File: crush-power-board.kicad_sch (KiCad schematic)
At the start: 17 parts, among them J1 Barrel_Jack, J2 1x2 Header, J3 Molex Micro Fit 3.0, J4 2157601008, J5 XT90PW-F

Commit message: Changed 5V regulator and 12V regulator to the SiC461. Both support 10A and 5V and 12V respectively
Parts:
- renumbered D3 to D1, D5 to D2, D4 to D3, D6 to D4, J5 to J1, J1 to J4, J4 to J5, R25 to R1, R28 to R2, R26 to R3, R27 to R4
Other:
- sheet 12V Regulator ports: added V_IN; removed 5V_IN, PGOOD_12V, VIN
- sheet 3.3V Regulator ports: added V_IN; removed Vin
- sheet 3.3V Regulator Thruster Side ports: added V_IN; removed Vin
- sheet 5V Regulator ports: added V_IN; removed PGOOD_5V, Vin

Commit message: Added more to the layout of the 12V regulator as well as changed some capacitor footprints
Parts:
- J2: footprint Connector_PinHeader_2.54mm:PinHeader_1x02_P2.54mm_Horizontal -> Connector_PinHeader_2.54mm:PinHeader_1x02_P2.54mm_Vertical
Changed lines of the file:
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@@
       (effects (font (size 1.27 1.27)))
     )
-    (property "Footprint" "Connector_PinHeader_2.54mm:PinHeader_1x02_P2.54mm_Horizontal" (at 73.66 129.54 0)
+    (property "Footprint" "Connector_PinHeader_2.54mm:PinHeader_1x02_P2.54mm_Vertical" (at 73.66 129.54 0)
       (effects (font (size 1.27 1.27)) hide)
     )

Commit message: fix batt_t planes
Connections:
- net +BATT: no longer J5.6
- net GND: no longer J5.8, R2.2
- new net +BATT_T: J5.6
- new net GND1: J5.8, R2.2
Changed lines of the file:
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@@
-    )
-  )
-  (symbol (lib_id "power:GND") (at 135.89 135.89 0) (unit 1)
-    (in_bom yes) (on_board yes) (dnp no) (fields_autoplaced)
-    (property "Reference" "#PWR018" (at 135.89 142.24 0)
-      (effects (font (size 1.27 1.27)) hide)
-    )
-    (property "Value" "GND_T" (at 135.89 140.97 0)
-      (effects (font (size 1.27 1.27)))
-    )
-    (property "Footprint" "" (at 135.89 135.89 0)
-      (effects (font (size 1.27 1.27)) hide)
-    )
-    (property "Datasheet" "" (at 135.89 135.89 0)
-      (effects (font (size 1.27 1.27)) hide)
-    )
-    (pin "1")
-    (instances
-      (project "crush-power-board"
-        (path "/530b9f5d-4c5f-47a4-a889-3cce870d311f"
-          (reference "#PWR018") (unit 1)
-        )
-      )
     )
   )
@@
         (path "/530b9f5d-4c5f-47a4-a889-3cce870d311f"
           (reference "R4") (unit 1)
-        )
-      )
-    )
-  )
-  (symbol (lib_id "power:+BATT") (at 137.16 104.14 0) (unit 1)
-    (in_bom yes) (on_board yes) (dnp no) (fields_autoplaced)
-    (property "Reference" "#PWR019" (at 137.16 107.95 0)
-      (effects (font (size 1.27 1.27)) hide)
-    )
-    (property "Value" "+BATT_T" (at 137.16 100.33 0)
-      (effects (font (size 1.27 1.27)))
-    )
-    (property "Footprint" "" (at 137.16 104.14 0)
-      (effects (font (size 1.27 1.27)) hide)
-    )
-    (property "Datasheet" "" (at 137.16 104.14 0)
-      (effects (font (size 1.27 1.27)) hide)
-    )
-    (pin "1")
-    (instances
-      (project "crush-power-board"
-        (path "/530b9f5d-4c5f-47a4-a889-3cce870d311f"
-          (reference "#PWR019") (unit 1)
         )
       )
@@
     )
   )
-  (symbol (lib_id "power:+BATT") (at 25.4 63.5 0) (unit 1)
-    (in_bom yes) (on_board yes) (dnp no) (fields_autoplaced)
-    (property "Reference" "#PWR05" (at 25.4 67.31 0)
-      (effects (font (size 1.27 1.27)) hide)
-    )
-    (property "Value" "+BATT_T" (at 25.4 59.69 0)
+  (symbol (lib_id "power:GND") (at 91.44 115.57 0) (unit 1)
+    (in_bom yes) (on_board yes) (dnp no) (fields_autoplaced)
+    (property "Reference" "#PWR011" (at 91.44 121.92 0)
+      (effects (font (size 1.27 1.27)) hide)
+    )
+    (property "Value" "GND" (at 91.44 120.65 0)
+      (effects (font (size 1.27 1.27)))
+    )
+    (property "Footprint" "" (at 91.44 115.57 0)
+      (effects (font (size 1.27 1.27)) hide)
+    )
+    (property "Datasheet" "" (at 91.44 115.57 0)
+      (effects (font (size 1.27 1.27)) hide)
+    )
+    (pin "1")
+    (instances
+      (project "crush-power-board"
+        (path "/530b9f5d-4c5f-47a4-a889-3cce870d311f"
+          (reference "#PWR011") (unit 1)
+        )
+      )
+    )
+  )
+  (symbol (lib_id "crush-power-lib:+BATT_T") (at 25.4 63.5 0) (unit 1)
+    (in_bom yes) (on_board yes) (dnp no) (fields_autoplaced)
+    (property "Reference" "#PWR019" (at 25.4 67.31 0)
+      (effects (font (size 1.27 1.27)) hide)
+    )
+    (property "Value" "+BATT_T" (at 25.4 58.42 0)
       (effects (font (size 1.27 1.27)))
     )
@@
       (project "crush-power-board"
         (path "/530b9f5d-4c5f-47a4-a889-3cce870d311f"
-          (reference "#PWR05") (unit 1)
-        )
-      )
-    )
-  )
-  (symbol (lib_id "power:GND") (at 91.44 115.57 0) (unit 1)
-    (in_bom yes) (on_board yes) (dnp no) (fields_autoplaced)
-    (property "Reference" "#PWR011" (at 91.44 121.92 0)
-      (effects (font (size 1.27 1.27)) hide)
-    )
-    (property "Value" "GND" (at 91.44 120.65 0)
-      (effects (font (size 1.27 1.27)))
-    )
-    (property "Footprint" "" (at 91.44 115.57 0)
-      (effects (font (size 1.27 1.27)) hide)
-    )
-    (property "Datasheet" "" (at 91.44 115.57 0)
-      (effects (font (size 1.27 1.27)) hide)
-    )
-    (pin "1")
-    (instances
-      (project "crush-power-board"
-        (path "/530b9f5d-4c5f-47a4-a889-3cce870d311f"
-          (reference "#PWR011") (unit 1)
-        )
-      )
-    )
-  )
-  (symbol (lib_id "power:GND") (at 24.13 148.59 0) (unit 1)
-    (in_bom yes) (on_board yes) (dnp no) (fields_autoplaced)
-    (property "Reference" "#PWR02" (at 24.13 154.94 0)
-      (effects (font (size 1.27 1.27)) hide)
-    )
-    (property "Value" "GND_T" (at 24.13 153.67 0)
-      (effects (font (size 1.27 1.27)))
-    )
-    (property "Footprint" "" (at 24.13 148.59 0)
-      (effects (font (size 1.27 1.27)) hide)
-    )
-    (property "Datasheet" "" (at 24.13 148.59 0)
-      (effects (font (size 1.27 1.27)) hide)
-    )
-    (pin "1")
-    (instances
-      (project "crush-power-board"
-        (path "/530b9f5d-4c5f-47a4-a889-3cce870d311f"
-          (reference "#PWR02") (unit 1)
+          (reference "#PWR019") (unit 1)
         )
       )
@@
     )
   )
-  (symbol (lib_id "power:GND") (at 25.4 81.28 0) (unit 1)
-    (in_bom yes) (on_board yes) (dnp no) (fields_autoplaced)
-    (property "Reference" "#PWR06" (at 25.4 87.63 0)
-      (effects (font (size 1.27 1.27)) hide)
-    )
-    (property "Value" "GND_T" (at 25.4 86.36 0)
-      (effects (font (size 1.27 1.27)))
-    )
-    (property "Footprint" "" (at 25.4 81.28 0)
-      (effects (font (size 1.27 1.27)) hide)
-    )
-    (property "Datasheet" "" (at 25.4 81.28 0)
-      (effects (font (size 1.27 1.27)) hide)
-    )
-    (pin "1")
-    (instances
-      (project "crush-power-board"
-        (path "/530b9f5d-4c5f-47a4-a889-3cce870d311f"
-          (reference "#PWR06") (unit 1)
-        )
-      )
-    )
-  )
   (symbol (lib_id "power:+BATT") (at 168.91 21.59 0) (unit 1)
     (in_bom yes) (on_board yes) (dnp no) (fields_autoplaced)
@@
         (path "/530b9f5d-4c5f-47a4-a889-3cce870d311f"
           (reference "#PWR020") (unit 1)
+        )
+      )
+    )
+  )
+  (symbol (lib_id "power:GND1") (at 135.89 135.89 0) (unit 1)
+    (in_bom yes) (on_board yes) (dnp no) (fields_autoplaced)
+    (property "Reference" "#PWR02" (at 135.89 142.24 0)
+      (effects (font (size 1.27 1.27)) hide)
+    )
+    (property "Value" "GND_T" (at 135.89 140.97 0)
+      (effects (font (size 1.27 1.27)))
+    )
+    (property "Footprint" "" (at 135.89 135.89 0)
+      (effects (font (size 1.27 1.27)) hide)
+    )
+    (property "Datasheet" "" (at 135.89 135.89 0)
+      (effects (font (size 1.27 1.27)) hide)
+    )
+    (pin "1")
+    (instances
+      (project "crush-power-board"
+        (path "/530b9f5d-4c5f-47a4-a889-3cce870d311f"
+          (reference "#PWR02") (unit 1)
+        )
+      )
+    )
+  )
+  (symbol (lib_id "power:GND1") (at 24.13 148.59 0) (unit 1)
+    (in_bom yes) (on_board yes) (dnp no) (fields_autoplaced)
+    (property "Reference" "#PWR023" (at 24.13 154.94 0)
+      (effects (font (size 1.27 1.27)) hide)
+    )
+    (property "Value" "GND_T" (at 24.13 153.67 0)
+      (effects (font (size 1.27 1.27)))
+    )
+    (property "Footprint" "" (at 24.13 148.59 0)
+      (effects (font (size 1.27 1.27)) hide)
+    )
+    (property "Datasheet" "" (at 24.13 148.59 0)
+      (effects (font (size 1.27 1.27)) hide)
+    )
+    (pin "1")
+    (instances
+      (project "crush-power-board"
+        (path "/530b9f5d-4c5f-47a4-a889-3cce870d311f"
+          (reference "#PWR023") (unit 1)
         )
       )
@@
         )
       )
+    )
+  )
+  (symbol (lib_id "crush-power-lib:+BATT_T") (at 137.16 104.14 0) (unit 1)
+    (in_bom yes) (on_board yes) (dnp no) (fields_autoplaced)
+    (property "Reference" "#PWR06" (at 137.16 107.95 0)
+      (effects (font (size 1.27 1.27)) hide)
+    )
+    (property "Value" "+BATT_T" (at 137.16 99.06 0)
+      (effects (font (size 1.27 1.27)))
+    )
+    (property "Footprint" "" (at 137.16 104.14 0)
+      (effects (font (size 1.27 1.27)) hide)
+    )
+    (property "Datasheet" "" (at 137.16 104.14 0)
+      (effects (font (size 1.27 1.27)) hide)
+    )
+    (pin "1")
+    (instances
+      (project "crush-power-board"
+        (path "/530b9f5d-4c5f-47a4-a889-3cce870d311f"
+          (reference "#PWR06") (unit 1)
+        )
+      )
+    )
+  )
+  (symbol (lib_id "power:GND1") (at 25.4 81.28 0) (unit 1)
+    (in_bom yes) (on_board yes) (dnp no) (fields_autoplaced)
+    (property "Reference" "#PWR018" (at 25.4 87.63 0)
+      (effects (font (size 1.27 1.27)) hide)
+    )
+    (property "Value" "GND_T" (at 25.4 86.36 0)
+      (effects (font (size 1.27 1.27)))
+    )
+    (property "Footprint" "" (at 25.4 81.28 0)
+      (effects (font (size 1.27 1.27)) hide)
+    )
+    (property "Datasheet" "" (at 25.4 81.28 0)
+      (effects (font (size 1.27 1.27)) hide)
+    )
+    (pin "1")
+    (instances
+      (project "crush-power-board"
+        (path "/530b9f5d-4c5f-47a4-a889-3cce870d311f"
+          (reference "#PWR018") (unit 1)
+        )
+      )

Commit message: added mounting holes
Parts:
- H1, H2, H3, H4: footprint (none) -> MountingHole:MountingHole_4.3mm_M4_Pad_Via
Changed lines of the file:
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@@
       (effects (font (size 1.27 1.27)) (justify left))
     )
-    (property "Footprint" "" (at 259.08 143.51 0)
+    (property "Footprint" "MountingHole:MountingHole_4.3mm_M4_Pad_Via" (at 259.08 143.51 0)
       (effects (font (size 1.27 1.27)) hide)
     )
@@
       (effects (font (size 1.27 1.27)) (justify left))
     )
-    (property "Footprint" "" (at 259.08 148.59 0)
+    (property "Footprint" "MountingHole:MountingHole_4.3mm_M4_Pad_Via" (at 259.08 148.59 0)
       (effects (font (size 1.27 1.27)) hide)
     )
@@
       (effects (font (size 1.27 1.27)) (justify left))
     )
-    (property "Footprint" "" (at 259.08 153.67 0)
+    (property "Footprint" "MountingHole:MountingHole_4.3mm_M4_Pad_Via" (at 259.08 153.67 0)
       (effects (font (size 1.27 1.27)) hide)
     )
@@
       (effects (font (size 1.27 1.27)) (justify left))
     )
-    (property "Footprint" "" (at 259.08 138.43 0)
-      (effects (font (size 1.27 1.27)) hide)
-    )
+    (property "Footprint" "MountingHole:MountingHole_4.3mm_M4_Pad_Via" (at 259.08 138.43 0)
+      (effects (font (size 1.27 1.27)) hide)
+    )

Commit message: use 6-32 mounting holes
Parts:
- H1, H2, H3, H4: footprint MountingHole:MountingHole_4.3mm_M4_Pad_Via -> MountingHole:MountingHole_3.7mm_Pad_Via
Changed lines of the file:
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@@
       (effects (font (size 1.27 1.27)) (justify left))
     )
-    (property "Footprint" "MountingHole:MountingHole_4.3mm_M4_Pad_Via" (at 259.08 143.51 0)
+    (property "Footprint" "MountingHole:MountingHole_3.7mm_Pad_Via" (at 259.08 143.51 0)
       (effects (font (size 1.27 1.27)) hide)
     )
@@
       (effects (font (size 1.27 1.27)) (justify left))
     )
-    (property "Footprint" "MountingHole:MountingHole_4.3mm_M4_Pad_Via" (at 259.08 148.59 0)
+    (property "Footprint" "MountingHole:MountingHole_3.7mm_Pad_Via" (at 259.08 148.59 0)
       (effects (font (size 1.27 1.27)) hide)
     )
@@
       (effects (font (size 1.27 1.27)) (justify left))
     )
-    (property "Footprint" "MountingHole:MountingHole_4.3mm_M4_Pad_Via" (at 259.08 153.67 0)
+    (property "Footprint" "MountingHole:MountingHole_3.7mm_Pad_Via" (at 259.08 153.67 0)
       (effects (font (size 1.27 1.27)) hide)
     )
@@
       (effects (font (size 1.27 1.27)) (justify left))
     )
-    (property "Footprint" "MountingHole:MountingHole_4.3mm_M4_Pad_Via" (at 259.08 138.43 0)
-      (effects (font (size 1.27 1.27)) hide)
-    )
+    (property "Footprint" "MountingHole:MountingHole_3.7mm_Pad_Via" (at 259.08 138.43 0)
+      (effects (font (size 1.27 1.27)) hide)
+    )

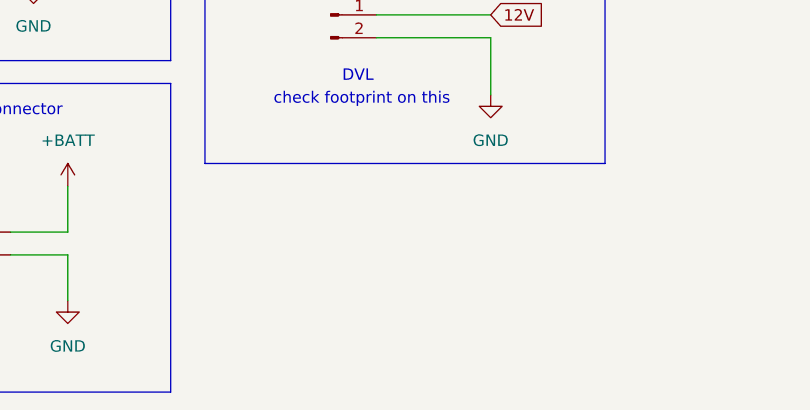
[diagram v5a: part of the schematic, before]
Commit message: add thruster battery connection
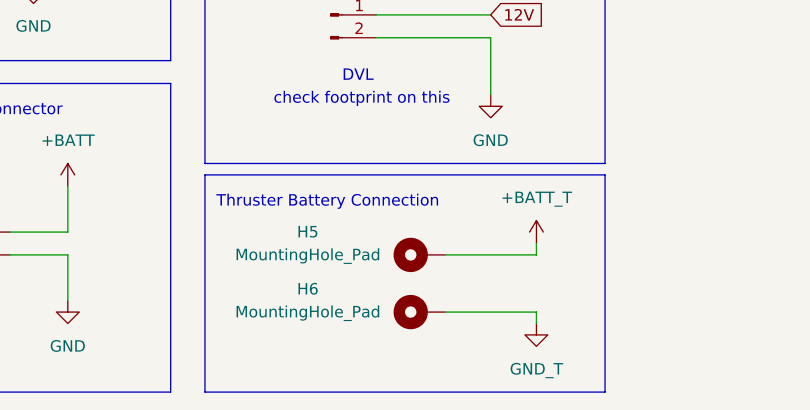
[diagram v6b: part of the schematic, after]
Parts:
- added H5, H6: MountingHole_Pad, MountingHole:MountingHole_5.5mm_Pad_Via, symbol Mechanical:MountingHole_Pad
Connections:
- net +BATT_T: now also H5.1
- net GND1: now also H6.1
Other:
- note added: "Thruster Battery Connection"
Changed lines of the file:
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@@
+    (stroke (width 0) (type default))
+  )
+  (wire (pts (xy 96.52 185.42) (xy 96.52 186.69))
     (stroke (width 0) (type default))
   )
@@
     (stroke (width 0) (type default))
   )
+  (wire (pts (xy 86.36 185.42) (xy 96.52 185.42))
+    (stroke (width 0) (type default))
+  )
   (wire (pts (xy 125.73 119.38) (xy 125.73 121.92))
     (stroke (width 0) (type default))
@@
     (stroke (width 0) (type default))
   )
+  (wire (pts (xy 86.36 179.07) (xy 96.52 179.07))
+    (stroke (width 0) (type default))
+  )
   (wire (pts (xy 99.06 33.02) (xy 109.22 33.02))
     (stroke (width 0) (type default))
   )
+  (wire (pts (xy 96.52 179.07) (xy 96.52 177.8))
+    (stroke (width 0) (type default))
+  )
   (wire (pts (xy 135.89 129.54) (xy 135.89 135.89))
     (stroke (width 0) (type default))
@@
   (wire (pts (xy 139.7 119.38) (xy 125.73 119.38))
     (stroke (width 0) (type default))
+  )
+  (rectangle (start 59.69 170.18) (end 104.14 194.31)
+    (stroke (width 0) (type default))
+    (fill (type none))
   )
   (rectangle (start 12.7 90.17) (end 55.88 157.48)
@@
   )
   (text "XT90 Battery Connector\n" (at 22.86 163.83 0)
+    (effects (font (size 1.27 1.27)) (justify left bottom))
+  )
+  (text "Thruster Battery Connection" (at 60.96 173.99 0)
     (effects (font (size 1.27 1.27)) (justify left bottom))
   )
@@
     )
   )
+  (symbol (lib_id "Mechanical:MountingHole_Pad") (at 83.82 185.42 90) (unit 1)
+    (in_bom yes) (on_board yes) (dnp no)
+    (property "Reference" "H6" (at 71.12 182.88 90)
+      (effects (font (size 1.27 1.27)))
+    )
+    (property "Value" "MountingHole_Pad" (at 71.12 185.42 90)
+      (effects (font (size 1.27 1.27)))
+    )
+    (property "Footprint" "MountingHole:MountingHole_5.5mm_Pad_Via" (at 83.82 185.42 0)
+      (effects (font (size 1.27 1.27)) hide)
+    )
+    (property "Datasheet" "~" (at 83.82 185.42 0)
+      (effects (font (size 1.27 1.27)) hide)
+    )
+    (pin "1")
+    (instances
+      (project "crush-power-board"
+        (path "/530b9f5d-4c5f-47a4-a889-3cce870d311f"
+          (reference "H6") (unit 1)
+        )
+      )
+    )
+  )
+  (symbol (lib_id "crush-power-lib:+BATT_T") (at 96.52 177.8 0) (unit 1)
+    (in_bom yes) (on_board yes) (dnp no) (fields_autoplaced)
+    (property "Reference" "#PWR05" (at 96.52 181.61 0)
+      (effects (font (size 1.27 1.27)) hide)
+    )
+    (property "Value" "+BATT_T" (at 96.52 172.72 0)
+      (effects (font (size 1.27 1.27)))
+    )
+    (property "Footprint" "" (at 96.52 177.8 0)
+      (effects (font (size 1.27 1.27)) hide)
+    )
+    (property "Datasheet" "" (at 96.52 177.8 0)
+      (effects (font (size 1.27 1.27)) hide)
+    )
+    (pin "1")
+    (instances
+      (project "crush-power-board"
+        (path "/530b9f5d-4c5f-47a4-a889-3cce870d311f"
+          (reference "#PWR05") (unit 1)
+        )
+      )
+    )
+  )
   (symbol (lib_id "crush-power-lib:+BATT_T") (at 25.4 63.5 0) (unit 1)
     (in_bom yes) (on_board yes) (dnp no) (fields_autoplaced)
@@
         )
       )
+    )
+  )
+  (symbol (lib_id "power:GND1") (at 96.52 186.69 0) (unit 1)
+    (in_bom yes) (on_board yes) (dnp no) (fields_autoplaced)
+    (property "Reference" "#PWR024" (at 96.52 193.04 0)
+      (effects (font (size 1.27 1.27)) hide)
+    )
+    (property "Value" "GND_T" (at 96.52 191.77 0)
+      (effects (font (size 1.27 1.27)))
+    )
+    (property "Footprint" "" (at 96.52 186.69 0)
+      (effects (font (size 1.27 1.27)) hide)
+    )
+    (property "Datasheet" "" (at 96.52 186.69 0)
+      (effects (font (size 1.27 1.27)) hide)
+    )
+    (pin "1")
+    (instances
+      (project "crush-power-board"
+        (path "/530b9f5d-4c5f-47a4-a889-3cce870d311f"
+          (reference "#PWR024") (unit 1)
+        )
+      )
+    )
+  )
+  (symbol (lib_id "Mechanical:MountingHole_Pad") (at 83.82 179.07 90) (unit 1)
+    (in_bom yes) (on_board yes) (dnp no)
+    (property "Reference" "H5" (at 71.12 176.53 90)
+      (effects (font (size 1.27 1.27)))
+    )
+    (property "Value" "MountingHole_Pad" (at 71.12 179.07 90)
+      (effects (font (size 1.27 1.27)))
+    )
+    (property "Footprint" "MountingHole:MountingHole_5.5mm_Pad_Via" (at 83.82 179.07 0)
+      (effects (font (size 1.27 1.27)) hide)
+    )
+    (property "Datasheet" "~" (at 83.82 179.07 0)
+      (effects (font (size 1.27 1.27)) hide)
+    )
+    (pin "1")
+    (instances
+      (project "crush-power-board"
+        (path "/530b9f5d-4c5f-47a4-a889-3cce870d311f"
+          (reference "H5") (unit 1)
+        )
+      )

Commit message: update for 8-32 screws
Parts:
- H5, H6: footprint MountingHole:MountingHole_5.5mm_Pad_Via -> MountingHole:MountingHole_4.5mm_Pad_Via
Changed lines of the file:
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@@
       (effects (font (size 1.27 1.27)))
     )
-    (property "Footprint" "MountingHole:MountingHole_5.5mm_Pad_Via" (at 83.82 185.42 0)
+    (property "Footprint" "MountingHole:MountingHole_4.5mm_Pad_Via" (at 83.82 185.42 0)
       (effects (font (size 1.27 1.27)) hide)
     )
@@
       (effects (font (size 1.27 1.27)))
     )
-    (property "Footprint" "MountingHole:MountingHole_5.5mm_Pad_Via" (at 83.82 179.07 0)
+    (property "Footprint" "MountingHole:MountingHole_4.5mm_Pad_Via" (at 83.82 179.07 0)
       (effects (font (size 1.27 1.27)) hide)
     )

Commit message: Added -5V voltage source using 5V regulator, also fixed 3V3 output pins on 3V3 regulator subsheets
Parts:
- added D7: LED_GREEN, LED_SMD:LED_0603_1608Metric, symbol Device:LED
- added R50: 100R, Resistor_SMD:R_0603_1608Metric, symbol Device:R_US
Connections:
- net GND: no longer J5.4
- new net: D7.1 (K), R50.2
- new net -5V: J5.4, R50.1
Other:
- added sheet -5V Regulator (neg_5v_reg.kicad_sch)
- moved on the sheet: H5, H6, J2, J3, J4, J5
